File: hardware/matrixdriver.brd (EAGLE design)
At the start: 52 x 51.4 mm, 34 parts, among them IC1 75176AD, IC2 4017D, IC3 ULN2803, IC4 7805DT, J1 DCJ0202, Q10 20MHZ, Q2 MMBT4403LT1SMD, Q3 MMBT4403LT1SMD, Q4 MMBT4403LT1SMD, Q5 MMBT4403LT1SMD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

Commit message: working on finishing
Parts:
- removed TP1: TPSQTP20R, testpad:TP20R
- added +: TPSQTP20R, testpad:TP20R
- added C5: 100n, resistor:C1206
- U$1: value TINY2313 -> 2313
- moved TP3 6.58 mm to (1.45, 26.7)
- moved TP2 5.38 mm to (1.40, 31.8)
- moved TP5 2.16 mm to (1.44, 24.1)
- moved TP4 1.73 mm to (1.45, 29.2)
- moved TP6 1.73 mm to (1.45, 21.6)
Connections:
- net GND: now also C5.1
- net N$7: now also +.TP; no longer TP1.TP
- net VCC: now also C5.2
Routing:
- net N$8: track 18.1 -> 11.3 mm
- net VCC: track 167.6 -> 171.6 mm
- net N$7: track 34.4 -> 30.8 mm
- net N$6: track 13.6 -> 15.3 mm
- net N$18: track 18.5 -> 19.6 mm
- net N$60: track 14.1 -> 13.2 mm
- net N$38: track 8.36 -> 9.20 mm
- net N$53: track 6.29 -> 6.96 mm
- net N$59: track 17.1 -> 17.7 mm

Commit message: working on board finalisation
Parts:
- removed C3: 100µ, rcl:UD-6,3X5,8_NICHICON
- added C6: 100UF, Panasonic-EEEFT_EEEH:CAPAE660X800N
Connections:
- net GND: now also C6.2; no longer C3.-
- net N$65: now also C6.1; no longer C3.+
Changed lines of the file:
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@@
 <setting verticaltext="up"/>
 </settings>
-<grid distance="12.5" unitdist="mil" unit="mil" style="lines" multiple="1" display="yes" altdistance="25" altunitdist="mil" altunit="mil"/>
+<grid distance="12.5" unitdist="mil" unit="mil" style="lines" multiple="1" display="no" altdistance="25" altunitdist="mil" altunit="mil"/>
 <layers>
 <layer number="1" name="Top" color="4" fill="1" visible="yes" active="yes"/>
-<layer number="16" name="Bottom" color="1" fill="1" visible="yes" active="yes"/>
+<layer number="16" name="Bottom" color="1" fill="1" visible="no" active="yes"/>
 <layer number="17" name="Pads" color="2" fill="1" visible="yes" active="yes"/>
 <layer number="18" name="Vias" color="2" fill="1" visible="yes" active="yes"/>
 <layer number="19" name="Unrouted" color="6" fill="1" visible="yes" active="yes"/>
 <layer number="20" name="Dimension" color="15" fill="1" visible="no" active="yes"/>
-<layer number="21" name="tPlace" color="7" fill="1" visible="no" active="yes"/>
-<layer number="22" name="bPlace" color="7" fill="1" visible="yes" active="yes"/>
+<layer number="21" name="tPlace" color="7" fill="1" visible="yes" active="yes"/>
+<layer number="22" name="bPlace" color="7" fill="1" visible="no" active="yes"/>
 <layer number="23" name="tOrigins" color="15" fill="1" visible="yes" active="yes"/>
-<layer number="24" name="bOrigins" color="15" fill="1" visible="yes" active="yes"/>
+<layer number="24" name="bOrigins" color="15" fill="1" visible="no" active="yes"/>
 <layer number="25" name="tNames" color="7" fill="1" visible="yes" active="yes"/>
 <layer number="26" name="bNames" color="7" fill="1" visible="yes" active="yes"/>
@@
 <layer number="28" name="bValues" color="7" fill="1" visible="no" active="yes"/>
 <layer number="29" name="tStop" color="7" fill="3" visible="yes" active="yes"/>
-<layer number="30" name="bStop" color="7" fill="6" visible="yes" active="yes"/>
+<layer number="30" name="bStop" color="7" fill="6" visible="no" active="yes"/>
 <layer number="31" name="tCream" color="7" fill="4" visible="yes" active="yes"/>
-<layer number="32" name="bCream" color="7" fill="5" visible="yes" active="yes"/>
+<layer number="32" name="bCream" color="7" fill="5" visible="no" active="yes"/>
 <layer number="33" name="tFinish" color="6" fill="3" visible="yes" active="yes"/>
-<layer number="34" name="bFinish" color="6" fill="6" visible="yes" active="yes"/>
+<layer number="34" name="bFinish" color="6" fill="6" visible="no" active="yes"/>
 <layer number="35" name="tGlue" color="7" fill="4" visible="no" active="yes"/>
 <layer number="36" name="bGlue" color="7" fill="5" visible="no" active="yes"/>
 <layer number="37" name="tTest" color="7" fill="1" visible="yes" active="yes"/>
-<layer number="38" name="bTest" color="7" fill="1" visible="yes" active="yes"/>
+<layer number="38" name="bTest" color="7" fill="1" visible="no" active="yes"/>
 <layer number="39" name="tKeepout" color="4" fill="11" visible="yes" active="yes"/>
-<layer number="40" name="bKeepout" color="1" fill="11" visible="yes" active="yes"/>
+<layer number="40" name="bKeepout" color="1" fill="11" visible="no" active="yes"/>
 <layer number="41" name="tRestrict" color="4" fill="10" visible="yes" active="yes"/>
-<layer number="42" name="bRestrict" color="1" fill="10" visible="yes" active="yes"/>
+<layer number="42" name="bRestrict" color="1" fill="10" visible="no" active="yes"/>
 <layer number="43" name="vRestrict" color="2" fill="10" visible="yes" active="yes"/>
 <layer number="44" name="Drills" color="7" fill="1" visible="yes" active="yes"/>
@@
 <layer number="111" name="LPC17xx" color="7" fill="1" visible="yes" active="yes"/>
 <layer number="112" name="tSilk" color="7" fill="1" visible="yes" active="yes"/>
-<layer number="116" name="Patch_BOT" color="9" fill="4" visible="yes" active="yes"/>
+<layer number="116" name="Patch_BOT" color="9" fill="4" visible="no" active="yes"/>
 <layer number="121" name="_tsilk" color="7" fill="1" visible="yes" active="yes"/>
-<layer number="122" name="_bsilk" color="7" fill="1" visible="yes" active="yes"/>
+<layer number="122" name="_bsilk" color="7" fill="1" visible="no" active="yes"/>
 <layer number="123" name="tTestmark" color="7" fill="1" visible="yes" active="yes"/>
-<layer number="124" name="bTestmark" color="7" fill="1" visible="yes" active="yes"/>
+<layer number="124" name="bTestmark" color="7" fill="1" visible="no" active="yes"/>
 <layer number="125" name="_tNames" color="7" fill="1" visible="yes" active="yes"/>
-<layer number="126" name="_bNames" color="7" fill="1" visible="yes" active="yes"/>
+<layer number="126" name="_bNames" color="7" fill="1" visible="no" active="yes"/>
 <layer number="127" name="_tValues" color="7" fill="1" visible="yes" active="yes"/>
-<layer number="128" name="_bValues" color="7" fill="1" visible="yes" active="yes"/>
+<layer number="128" name="_bValues" color="7" fill="1" visible="no" active="yes"/>
 <layer number="131" name="tAdjust" color="7" fill="1" visible="no" active="yes"/>
 <layer number="132" name="bAdjust" color="7" fill="1" visible="no" active="yes"/>
@@
 Matrixdriver</text>
 <text x="49.53" y="9.525" size="1.016" layer="1" font="vector" rot="R270">REV 1</text>
-<hole x="1.5875" y="49.53" drill="0.6"/>
-<hole x="50.4825" y="1.905" drill="0.6"/>
-<hole x="50.4825" y="49.53" drill="0.6"/>
-<hole x="1.5875" y="1.905" drill="0.6"/>
+<hole x="1.905" y="49.53" drill="1.1"/>
+<hole x="50.165" y="1.905" drill="1.1"/>
+<hole x="49.8475" y="49.53" drill="1.1"/>
+<hole x="1.905" y="1.905" drill="1.1"/>
 </plain>
 <attributes>
@@
 <attribute name="VALUE" x="49.53" y="35.56" size="1.27" layer="27" rot="R180"/>
 </element>
-<element name="C3" library="rcl" package="UD-6,3X5,8_NICHICON" value="100µ" x="43.18" y="12.065" smashed="yes" rot="R180">
-<attribute name="VALUE" x="43.815" y="7.62" size="1.016" layer="27"/>
-</element>
 <element name="C4" library="rcl" package="C1206" value="10µ" x="45.085" y="17.78" smashed="yes">
 <attribute name="VALUE" x="49.2125" y="16.51" size="1.27" layer="27" rot="R90"/>
@@
 <element name="C5" library="resistor" package="C1206" value="100n" x="2.54" y="12.7" smashed="yes" rot="R90">
 <attribute name="VALUE" x="5.588" y="13.0175" size="1.27" layer="27" rot="R90"/>
+</element>
+<element name="C6" library="Panasonic-EEEFT_EEEH" package="CAPAE660X800N" value="100UF" x="43.18" y="12.065" smashed="yes">
+<attribute name="PACKAGE" value="CASE-D8" x="43.18" y="12.065" size="1.778" layer="27" display="off"/>
+<attribute name="OC_NEWARK" value="15R0909" x="43.18" y="12.065" size="1.778" layer="27" display="off"/>
+<attribute name="TOLERANCE" value="±20 %" x="43.18" y="12.065" size="1.778" layer="27" display="off"/>
+<attribute name="MPN" value="EEE-HC1C101XP" x="43.18" y="12.065" size="1.778" layer="27" display="off"/>
+<attribute name="SUPPLIER" value="PANASONIC" x="43.18" y="12.065" size="1.778" layer="27" display="off"/>
+<attribute name="VOLTAGERATING" value="16V" x="43.18" y="12.065" size="1.778" layer="27" display="off"/>
+<attribute name="OC_FARNELL" value="1714695  " x="43.18" y="12.065" size="1.778" layer="27" display="off"/>
 </element>
 </elements>
@@
 <contactref element="J1" pad="3"/>
 <contactref element="C4" pad="2"/>
-<contactref element="C3" pad="-"/>
 <contactref element="IC2" pad="8"/>
 <polygon width="0.4064" layer="16" isolate="0.003175">
@@
 <via x="34.925" y="27.305" extent="1-16" drill="0.6" shape="octagon"/>
 <via x="10.16" y="33.655" extent="1-16" drill="0.6"/>
+<contactref element="C6" pad="2"/>
 </signal>
 <signal name="N$15">
@@
 <signal name="N$65">
 <contactref element="IC4" pad="1"/>
-<contactref element="C3" pad="+"/>
 <contactref element="J1" pad="1"/>
 <wire x1="44.075" y1="32.03" x2="42.825" y2="32.03" width="0.4064" layer="1"/>
@@
 <wire x1="40.715" y1="29.285" x2="40.715" y2="24.13" width="0.4064" layer="1"/>
 <wire x1="40.715" y1="24.13" x2="41.91" y2="22.935" width="0.4064" layer="1"/>
-<wire x1="41.91" y1="22.935" x2="41.91" y2="13.335" width="0.4064" layer="1"/>
-<wire x1="41.91" y1="13.335" x2="40.83" y2="12.255" width="0.4064" layer="1"/>
-<wire x1="40.83" y1="12.255" x2="40.83" y2="12.065" width="0.4064" layer="1"/>
+<wire x1="41.91" y1="22.935" x2="41.91" y2="13.208" width="0.4064" layer="1"/>
+<contactref element="C6" pad="1"/>
+<wire x1="41.91" y1="13.208" x2="40.767" y2="12.065" width="0.4064" layer="1"/>
 </signal>
 <signal name="N$11">

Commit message: working on partlist
add numbers document with parts from digikey
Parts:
- removed Q10: 20MHZ, adafruit:HC49/S
- added Q1: 20MHZ, crystal:HC49UP
- moved C2 2.54 mm to (24.8, 5.08)
- moved JP4 1.27 mm to (24.8, 12.1)
- moved C1 0.95 mm to (6.03, 5.08)
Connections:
- net N$11: now also Q1.2; no longer Q10.2
- net N$12: now also Q1.1; no longer Q10.1
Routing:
- net N$12: track 14.1 -> 20.3 mm
- net N$57: track 33.9 -> 32.5 mm
- net N$61: track 15.3 -> 14.1 mm
- net N$62: track 17.7 -> 16.5 mm
- net N$9: track 48.4 -> 47.3 mm
- net N$10: track 62.6 -> 61.5 mm
- net N$60: track 13.2 -> 12.3 mm
- net N$40: track 14.0 -> 14.6 mm

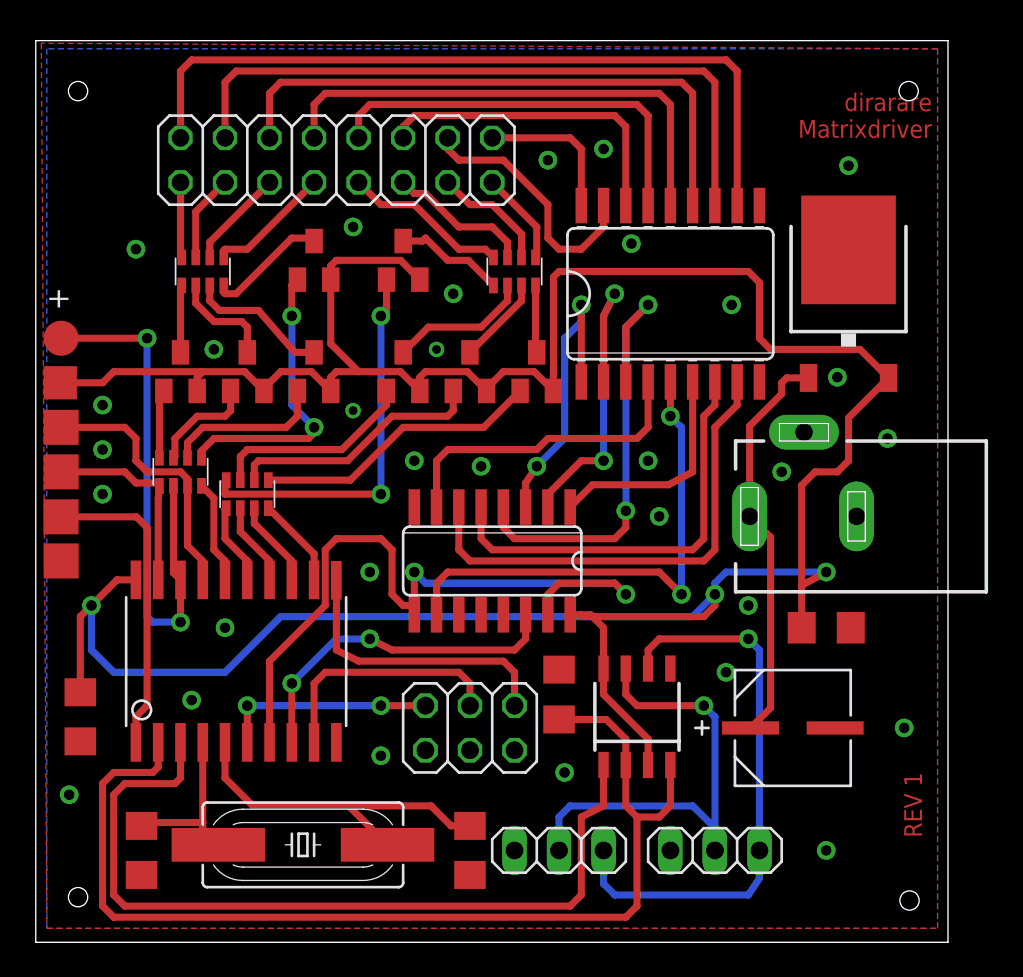
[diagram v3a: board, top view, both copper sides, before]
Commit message: fix some layout errors
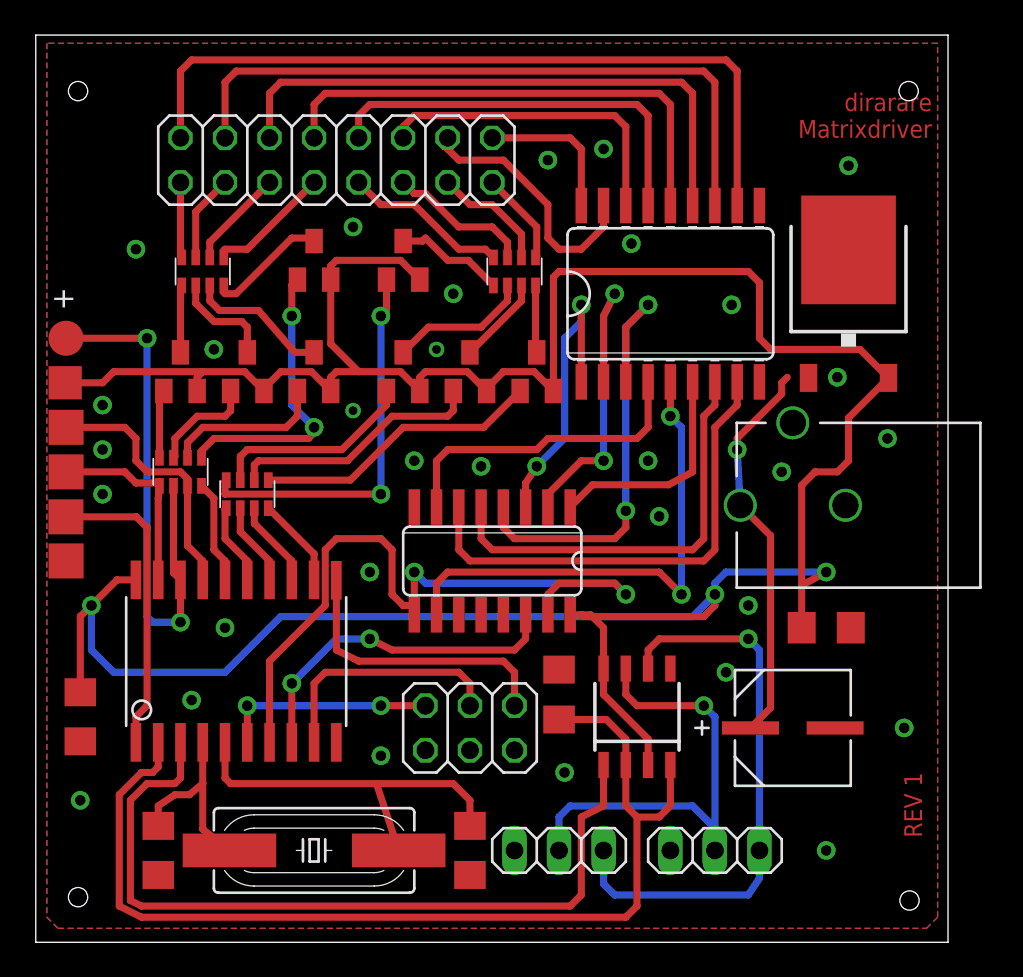
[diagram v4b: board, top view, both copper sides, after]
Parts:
- removed J1: DCJ0202, con-jack:DCJ0202
- added U$2: CUI_PJ-102A, con-dc-jack:CUI_DCJACK_PCB
- moved C1 0.95 mm to (6.99, 5.08)
- moved Q1 0.71 mm to (15.9, 5.08)
- moved + 0.28 mm to (1.73, 34.3)
- moved TP3 0.28 mm to (1.73, 26.7)
- moved TP4 0.28 mm to (1.73, 29.2), turned to 90 degrees
- moved TP5 0.28 mm to (1.72, 24.1)
- moved TP6 0.28 mm to (1.73, 21.6)
- moved TP2 0.28 mm to (1.68, 31.8)
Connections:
- new net FOO: U$2.CASE
- net GND: now also U$2.-; no longer J1.3
- net N$65: now also U$2.+; no longer J1.1
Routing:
- net N$10: track 61.5 -> 59.1 mm
- net N$9: track 47.3 -> 45.4 mm
- net N$12: track 20.3 -> 22.0 mm
- net N$11: track 9.78 -> 11.0 mm
- net N$65: track 23.1 -> 22.4 mm, vias 0 -> 1
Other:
- board size 52 x 51.4 mm -> 52 x 51.7 mm

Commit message: working on 50/50 board
- shrinking
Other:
- board size 52 x 51.7 mm -> 50 x 50 mm
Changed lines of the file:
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@@
 <setting verticaltext="up"/>
 </settings>
-<grid distance="12.5" unitdist="mil" unit="mil" style="lines" multiple="25" display="no" altdistance="25" altunitdist="mil" altunit="mil"/>
+<grid distance="12.5" unitdist="mil" unit="mm" style="lines" multiple="25" display="no" altdistance="25" altunitdist="mil" altunit="mm"/>
 <layers>
 <layer number="1" name="Top" color="4" fill="1" visible="yes" active="yes"/>
@@
 <board>
 <plain>
-<wire x1="0" y1="-0.16" x2="52.03" y2="-0.16" width="0" layer="20"/>
-<wire x1="52.03" y1="-0.16" x2="52.03" y2="51.5825" width="0" layer="20"/>
-<wire x1="52.03" y1="51.5825" x2="0" y2="51.5825" width="0" layer="20"/>
-<wire x1="0" y1="51.5825" x2="0" y2="-0.16" width="0" layer="20"/>
+<wire x1="0" y1="0" x2="50" y2="0" width="0" layer="20"/>
+<wire x1="50" y1="0" x2="50" y2="50" width="0" layer="20"/>
+<wire x1="50" y1="50" x2="0" y2="50" width="0" layer="20"/>
+<wire x1="0" y1="50" x2="0" y2="0" width="0" layer="20"/>
 <text x="51.1175" y="48.26" size="1.016" layer="1" font="vector" rot="R180">dirarare
 Matrixdriver</text>

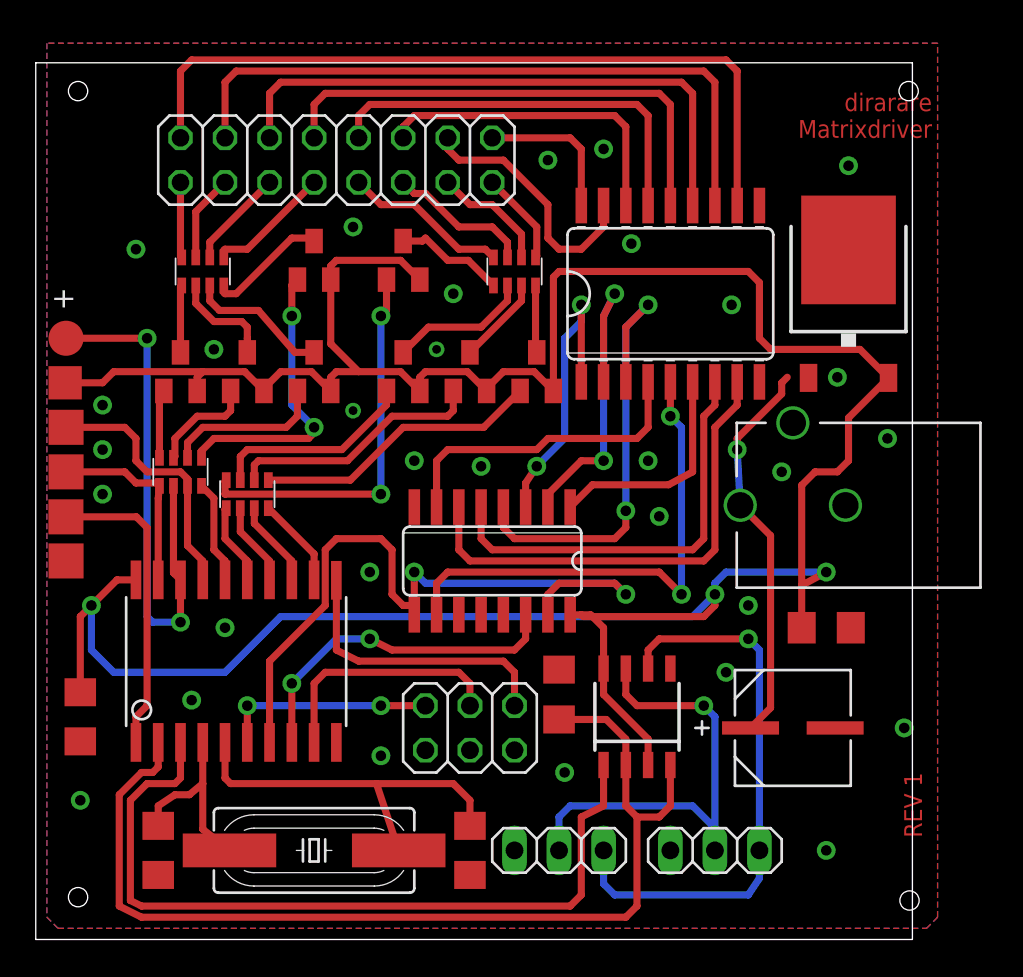
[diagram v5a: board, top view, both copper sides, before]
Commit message: resize to 5050
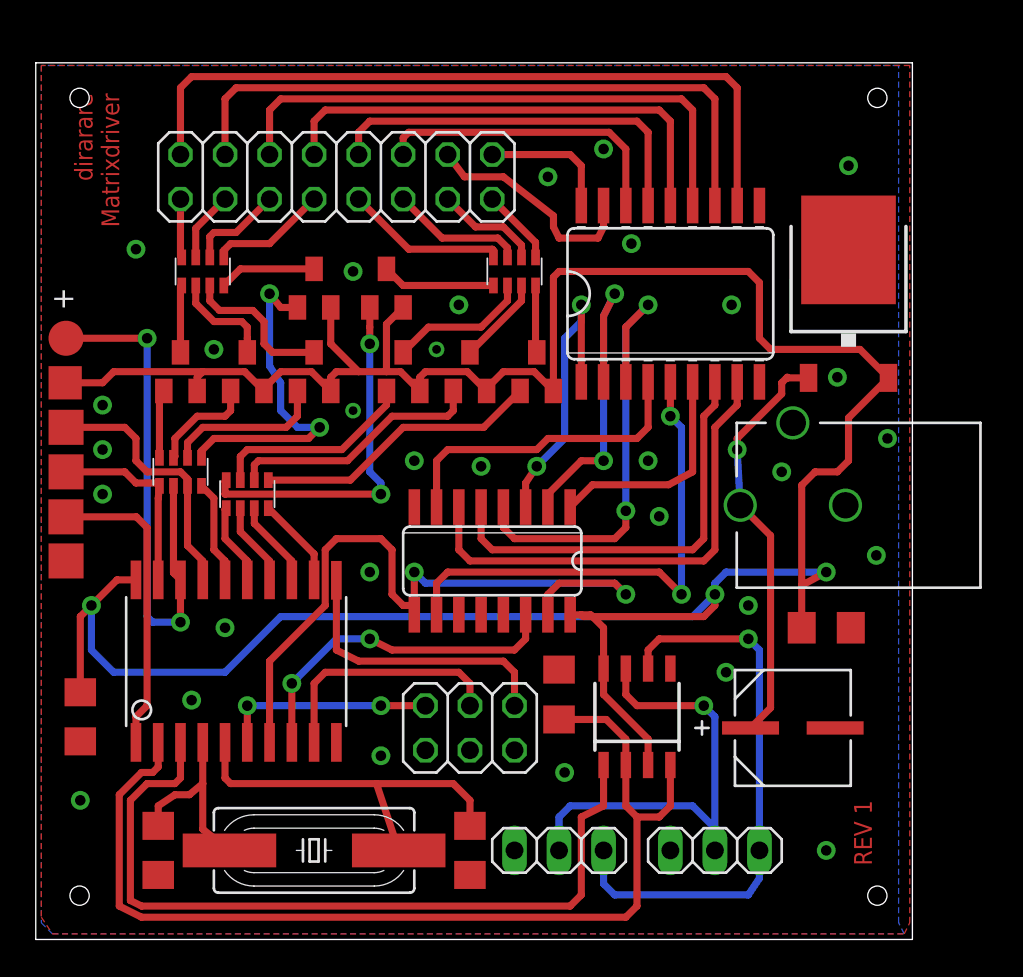
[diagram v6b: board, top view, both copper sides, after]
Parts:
- moved Q6 1.85 mm to (20.0, 37.1)
- moved Q5 1.59 mm to (15.9, 37.1)
- moved JP1 0.95 mm to (17.1, 43.5)
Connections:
- removed net FOO: U$2.CASE
- net GND: now also U$2.CASE
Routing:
- net VCC: track 171.4 -> 167.4 mm
- net N$39: track 16.6 -> 19.1 mm
- net N$26: track 14.8 -> 12.9 mm
- net N$42: track 22.1 -> 20.6 mm
- net N$53: track 6.96 -> 5.54 mm
- net N$65: track 22.4 -> 23.6 mm
- net N$31: track 5.36 -> 4.35 mm
- net N$25: track 8.57 -> 7.62 mm
- net N$66: track 28.5 -> 27.6 mm
- net N$64: track 33.6 -> 32.6 mm
- net N$63: track 38.7 -> 37.7 mm
- net N$34: track 4.97 -> 4.02 mm
- net N$33: track 4.31 -> 3.36 mm
- net N$28: track 23.4 -> 22.5 mm
- net N$27: track 18.4 -> 17.4 mm
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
